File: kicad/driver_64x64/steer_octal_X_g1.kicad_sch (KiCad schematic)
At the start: 66 parts

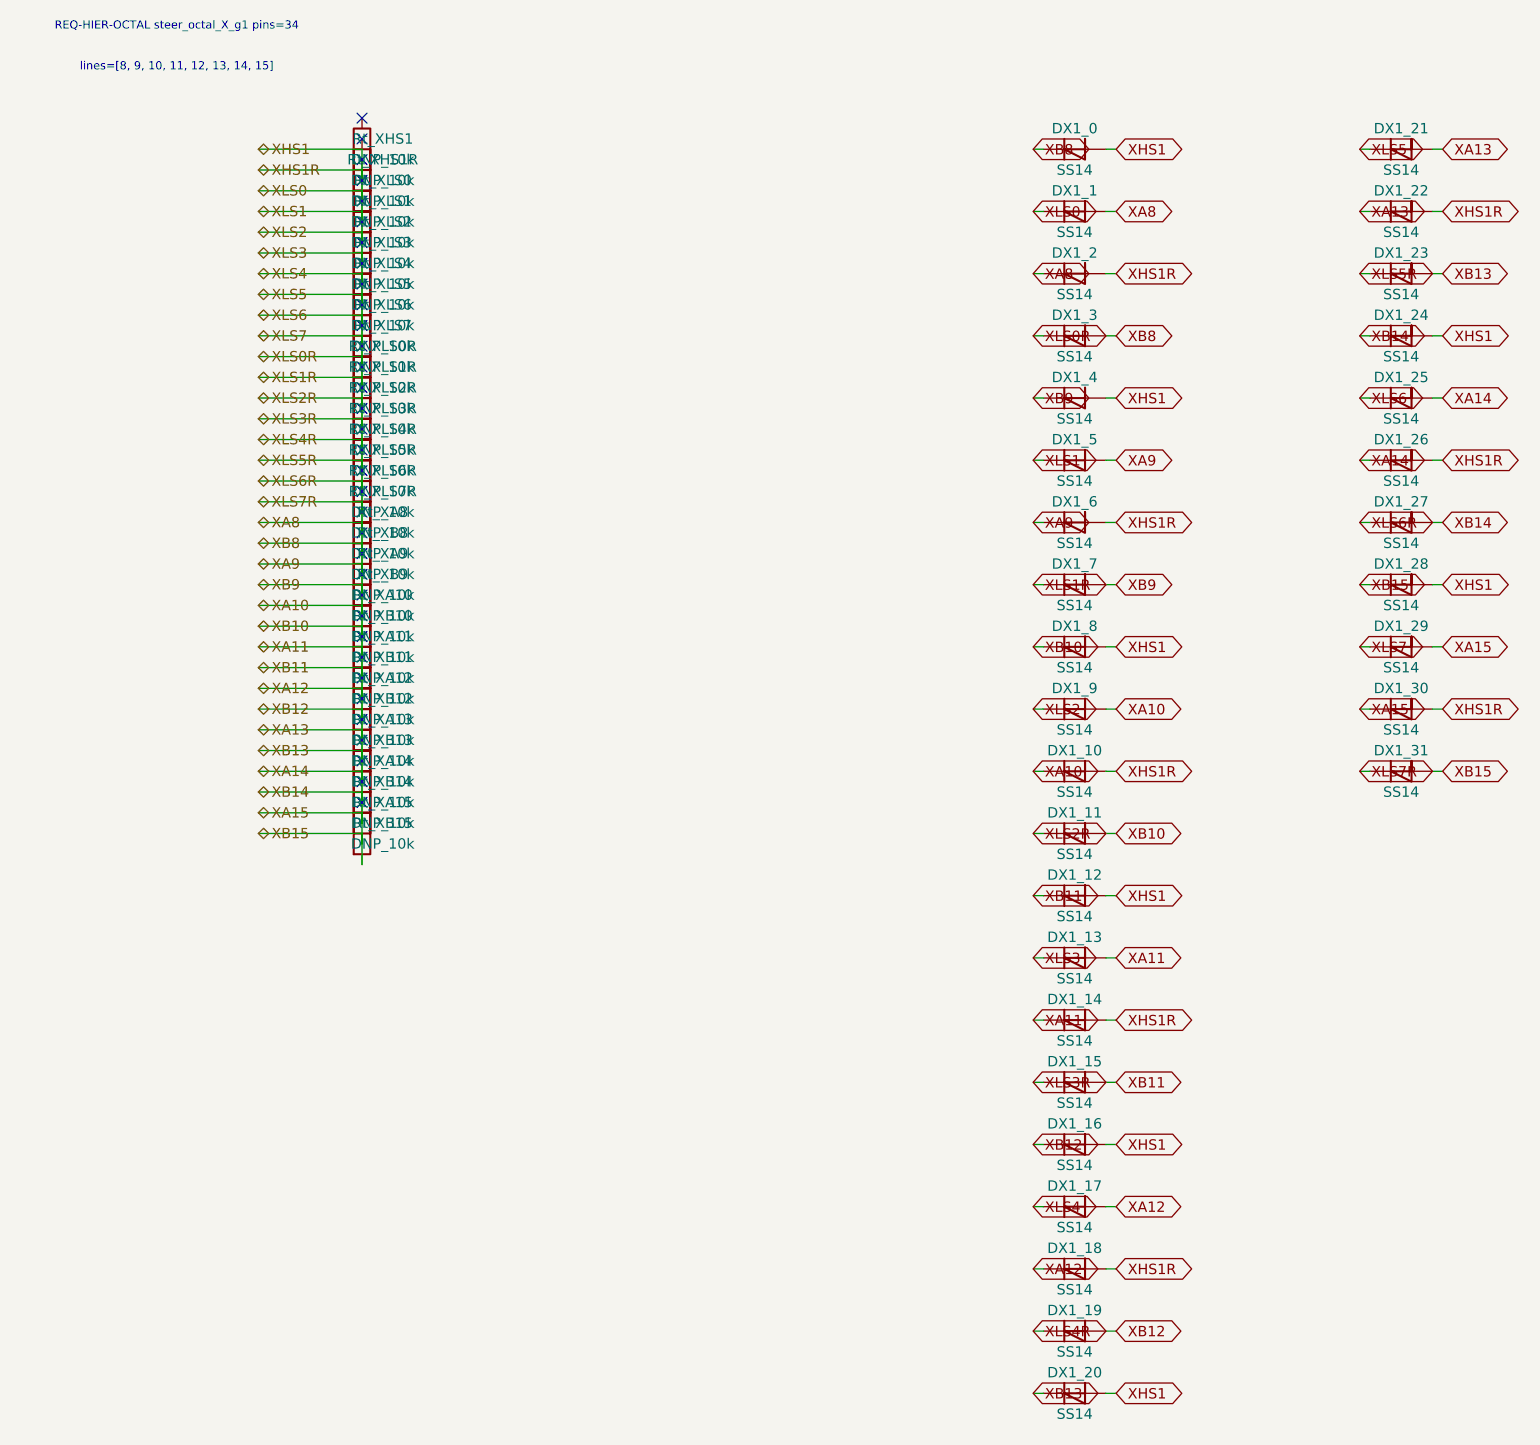
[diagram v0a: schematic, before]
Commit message: logical seperation into host and multiple decode/drive/steering boards
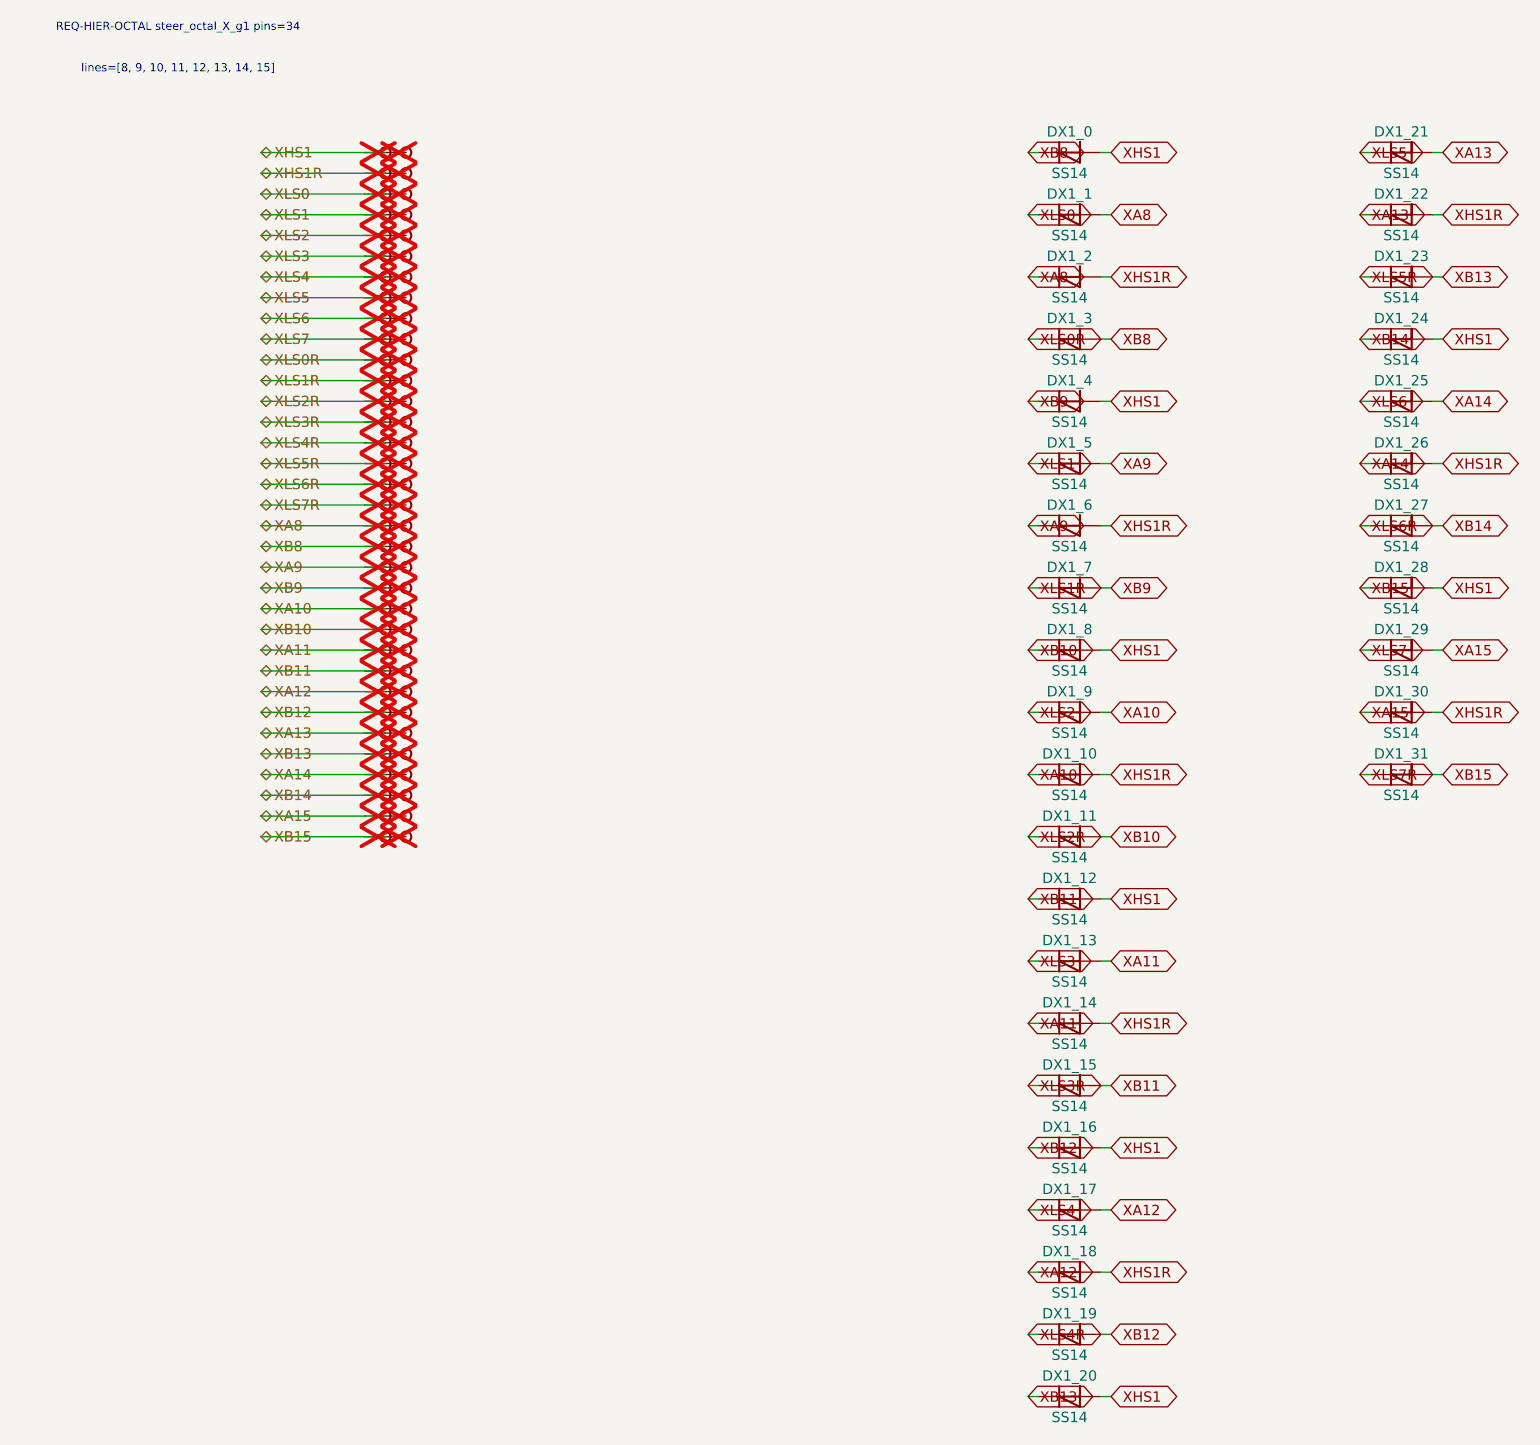
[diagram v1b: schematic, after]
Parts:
- removed Rt_XA10, Rt_XA11, Rt_XA12, Rt_XA13, Rt_XA14, Rt_XA15, Rt_XA8, Rt_XA9, Rt_XB10, Rt_XB11, Rt_XB12, Rt_XB13, Rt_XB14, Rt_XB15, Rt_XB8, Rt_XB9, Rt_XHS1, Rt_XHS1R, Rt_XLS0, Rt_XLS0R, Rt_XLS1, Rt_XLS1R, Rt_XLS2, Rt_XLS2R, Rt_XLS3, Rt_XLS3R, Rt_XLS4, Rt_XLS4R, Rt_XLS5, Rt_XLS5R, Rt_XLS6, Rt_XLS6R, Rt_XLS7, Rt_XLS7R: DNP_10k, symbol Device:R
- added TP_XA10, TP_XA10b, TP_XA11, TP_XA11b, TP_XA12, TP_XA12b, TP_XA13, TP_XA13b, TP_XA14, TP_XA14b, TP_XA15, TP_XA15b, TP_XA8, TP_XA8b, TP_XA9, TP_XA9b, TP_XB10, TP_XB10b, TP_XB11, TP_XB11b, TP_XB12, TP_XB12b, TP_XB13, TP_XB13b, TP_XB14, TP_XB14b, TP_XB15, TP_XB15b, TP_XB8, TP_XB8b, TP_XB9, TP_XB9b, TP_XHS1, TP_XHS1R, TP_XHS1Rb, TP_XHS1b, TP_XLS0, TP_XLS0R, TP_XLS0Rb, TP_XLS0b, TP_XLS1, TP_XLS1R, TP_XLS1Rb, TP_XLS1b, TP_XLS2, TP_XLS2R, TP_XLS2Rb, TP_XLS2b, TP_XLS3, TP_XLS3R, TP_XLS3Rb, TP_XLS3b, TP_XLS4, TP_XLS4R, TP_XLS4Rb, TP_XLS4b, TP_XLS5, TP_XLS5R, TP_XLS5Rb, TP_XLS5b, TP_XLS6, TP_XLS6R, TP_XLS6Rb, TP_XLS6b, TP_XLS7, TP_XLS7R, TP_XLS7Rb, TP_XLS7b: Stub, symbol CMR:Stub
- DX1_0, DX1_1, DX1_10, DX1_11, DX1_12, DX1_13, DX1_14, DX1_15, DX1_16, DX1_17, DX1_18, DX1_19, DX1_2, DX1_20, DX1_21, DX1_22, DX1_23, DX1_24, DX1_25, DX1_26, DX1_27, DX1_28, DX1_29, DX1_3, DX1_30, DX1_31, DX1_4, DX1_5, DX1_6, DX1_7, DX1_8, DX1_9: symbol Device:D_Schottky -> CMR:D_Schottky
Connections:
- net XA10: now also TP_XA10.1, TP_XA10b.1; no longer DX1_0.1 (K), DX1_0.2 (A), DX1_1.1 (K), DX1_1.2 (A), DX1_10.2 (A), DX1_11.1 (K), DX1_11.2 (A), DX1_12.1 (K), DX1_12.2 (A), DX1_13.1 (K), DX1_13.2 (A), DX1_14.1 (K), DX1_14.2 (A), DX1_15.1 (K), DX1_15.2 (A), DX1_16.1 (K), DX1_16.2 (A), DX1_17.1 (K), DX1_17.2 (A), DX1_18.1 (K), DX1_18.2 (A), DX1_19.1 (K), DX1_19.2 (A), DX1_2.1 (K), DX1_2.2 (A), DX1_20.1 (K), DX1_20.2 (A), DX1_21.1 (K), DX1_21.2 (A), DX1_22.1 (K), DX1_22.2 (A), DX1_23.1 (K), DX1_23.2 (A), DX1_24.1 (K), DX1_24.2 (A), DX1_25.1 (K), DX1_25.2 (A), DX1_26.1 (K), DX1_26.2 (A), DX1_27.1 (K), DX1_27.2 (A), DX1_28.1 (K), DX1_28.2 (A), DX1_29.1 (K), DX1_29.2 (A), DX1_3.1 (K), DX1_3.2 (A), DX1_30.1 (K), DX1_30.2 (A), DX1_31.1 (K), DX1_31.2 (A), DX1_4.1 (K), DX1_4.2 (A), DX1_5.1 (K), DX1_5.2 (A), DX1_6.1 (K), DX1_6.2 (A), DX1_7.1 (K), DX1_7.2 (A), DX1_8.1 (K), DX1_8.2 (A), DX1_9.1 (K)
- new net XA11: DX1_13.2 (A), DX1_14.1 (K), TP_XA11.1, TP_XA11b.1
- new net XA12: DX1_17.2 (A), DX1_18.1 (K), TP_XA12.1, TP_XA12b.1
- new net XA13: DX1_21.2 (A), DX1_22.1 (K), TP_XA13.1, TP_XA13b.1
- new net XA14: DX1_25.2 (A), DX1_26.1 (K), TP_XA14.1, TP_XA14b.1
- new net XA15: DX1_29.2 (A), DX1_30.1 (K), TP_XA15.1, TP_XA15b.1
- new net XA8: DX1_1.2 (A), DX1_2.1 (K), TP_XA8.1, TP_XA8b.1
- new net XA9: DX1_5.2 (A), DX1_6.1 (K), TP_XA9.1, TP_XA9b.1
- new net XB10: DX1_11.2 (A), DX1_8.1 (K), TP_XB10.1, TP_XB10b.1
- new net XB11: DX1_12.1 (K), DX1_15.2 (A), TP_XB11.1, TP_XB11b.1
- new net XB12: DX1_16.1 (K), DX1_19.2 (A), TP_XB12.1, TP_XB12b.1
- new net XB13: DX1_20.1 (K), DX1_23.2 (A), TP_XB13.1, TP_XB13b.1
- new net XB14: DX1_24.1 (K), DX1_27.2 (A), TP_XB14.1, TP_XB14b.1
- new net XB15: DX1_28.1 (K), DX1_31.2 (A), TP_XB15.1, TP_XB15b.1
- new net XB8: DX1_0.1 (K), DX1_3.2 (A), TP_XB8.1, TP_XB8b.1
- new net XB9: DX1_4.1 (K), DX1_7.2 (A), TP_XB9.1, TP_XB9b.1
- new net XHS1: DX1_0.2 (A), DX1_12.2 (A), DX1_16.2 (A), DX1_20.2 (A), DX1_24.2 (A), DX1_28.2 (A), DX1_4.2 (A), DX1_8.2 (A), TP_XHS1.1, TP_XHS1b.1
- new net XHS1R: DX1_10.2 (A), DX1_14.2 (A), DX1_18.2 (A), DX1_2.2 (A), DX1_22.2 (A), DX1_26.2 (A), DX1_30.2 (A), DX1_6.2 (A), TP_XHS1R.1, TP_XHS1Rb.1
- new net XLS0: DX1_1.1 (K), TP_XLS0.1, TP_XLS0b.1
- new net XLS0R: DX1_3.1 (K), TP_XLS0R.1, TP_XLS0Rb.1
- new net XLS1: DX1_5.1 (K), TP_XLS1.1, TP_XLS1b.1
- new net XLS1R: DX1_7.1 (K), TP_XLS1R.1, TP_XLS1Rb.1
- new net XLS2: DX1_9.1 (K), TP_XLS2.1, TP_XLS2b.1
- new net XLS2R: DX1_11.1 (K), TP_XLS2R.1, TP_XLS2Rb.1
- new net XLS3: DX1_13.1 (K), TP_XLS3.1, TP_XLS3b.1
- new net XLS3R: DX1_15.1 (K), TP_XLS3R.1, TP_XLS3Rb.1
- new net XLS4: DX1_17.1 (K), TP_XLS4.1, TP_XLS4b.1
- new net XLS4R: DX1_19.1 (K), TP_XLS4R.1, TP_XLS4Rb.1
- new net XLS5: DX1_21.1 (K), TP_XLS5.1, TP_XLS5b.1
- new net XLS5R: DX1_23.1 (K), TP_XLS5R.1, TP_XLS5Rb.1
- new net XLS6: DX1_25.1 (K), TP_XLS6.1, TP_XLS6b.1
- new net XLS6R: DX1_27.1 (K), TP_XLS6R.1, TP_XLS6Rb.1
- new net XLS7: DX1_29.1 (K), TP_XLS7.1, TP_XLS7b.1
- new net XLS7R: DX1_31.1 (K), TP_XLS7R.1, TP_XLS7Rb.1
- no-connect marks 34 -> 0
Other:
- moved on the sheet: DX1_0, DX1_1, DX1_10, DX1_11, DX1_12, DX1_13, DX1_14, DX1_15, DX1_16, DX1_17, DX1_18, DX1_19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
